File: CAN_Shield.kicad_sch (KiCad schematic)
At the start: 23 parts, among them J1 GPIO, U1 ATECC608A-SSHDA-T, U2 MCP2515T-I/SO, U4 SN65HVD230DR, X1 X322516MLB4SI, j2 DB128V-5.08-5P-GN-S, j3 DB128V-5.08-7P-GN-S, j4 DB128V-5.08-7P-GN-S

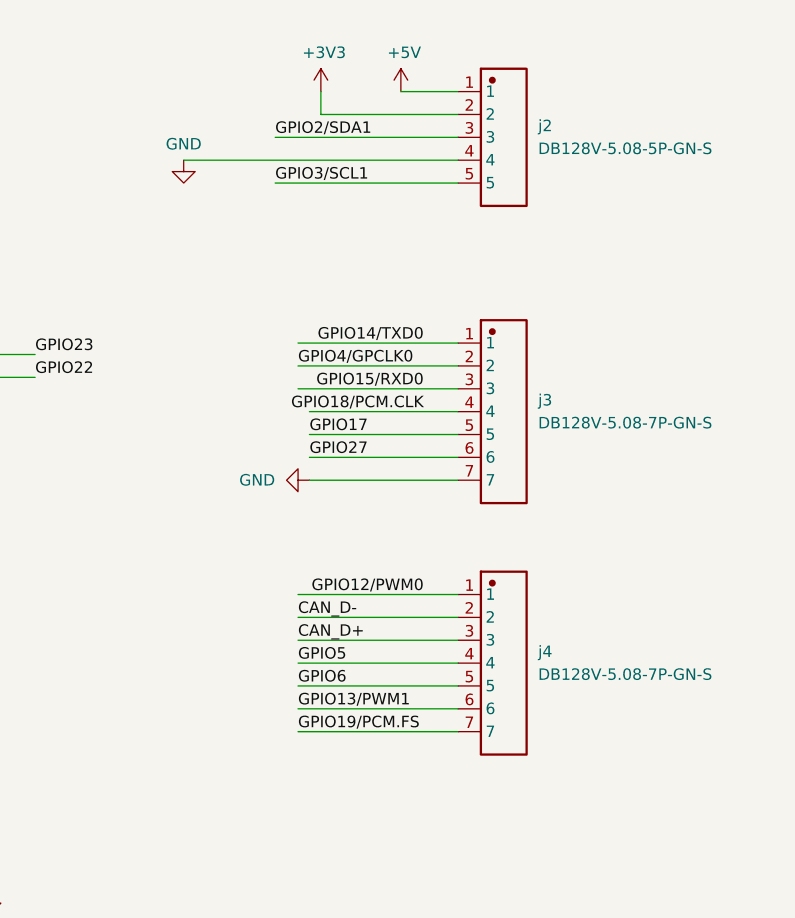
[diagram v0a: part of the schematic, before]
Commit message: Quick fix from EzSeperateI2C
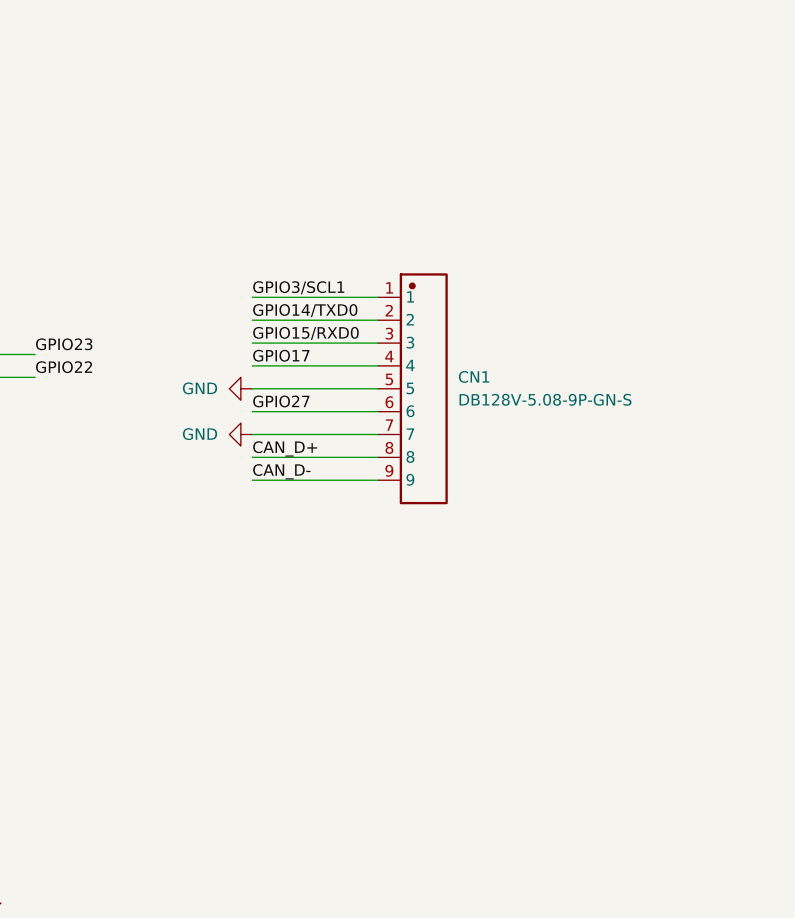
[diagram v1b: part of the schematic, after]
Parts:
- removed j2: DB128V-5.08-5P-GN-S, ImportFP:CONN-TH_5P-P5.08_DIBO_DB128V-5.08-5P-GN-S, symbol ImportSymbol:DB128V-5.08-5P-GN-S
- removed j3, j4: DB128V-5.08-7P-GN-S, ImportFP:CONN-TH_7P-P5.08_DIBO_DB128V-5.08-7P-GN-S, symbol ImportSymbol:DB128V-5.08-7P-GN-S
- added CN1: DB128V-5.08-9P-GN-S, ImportFP:CONN-TH_9P-P5.08_DIBO_DB128V-5.08-9P-GN-S, symbol ImportSymbol:DB128V-5.08-9P-GN-S
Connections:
- net CAN_D+: now also CN1.8
- net CAN_D-: now also CN1.9
- net GND: now also CN1.5, CN1.7
- net GPIO14/TXD0: now also CN1.2
- net GPIO15/RXD0: now also CN1.3
- net GPIO17: now also CN1.4
- net GPIO27: now also CN1.6
- net GPIO3/SCL1: now also CN1.1

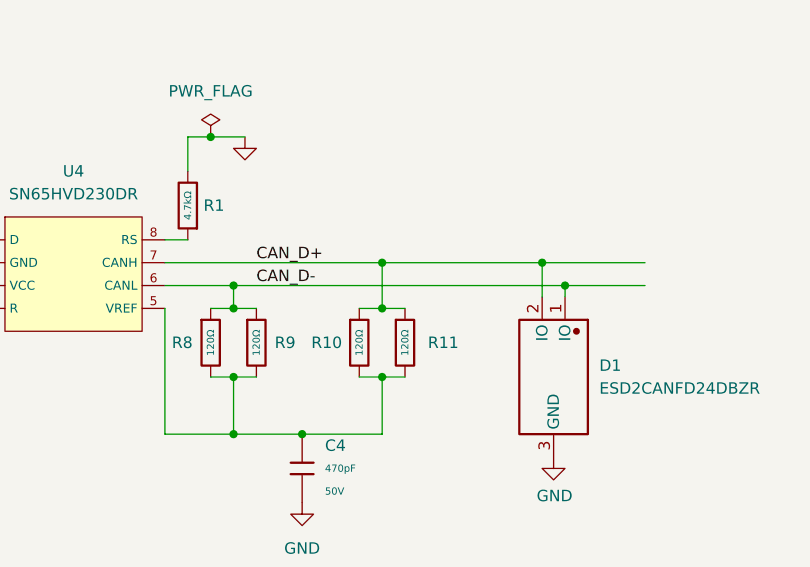
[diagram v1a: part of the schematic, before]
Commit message: Finished DesktopShield layout but still not gen production file
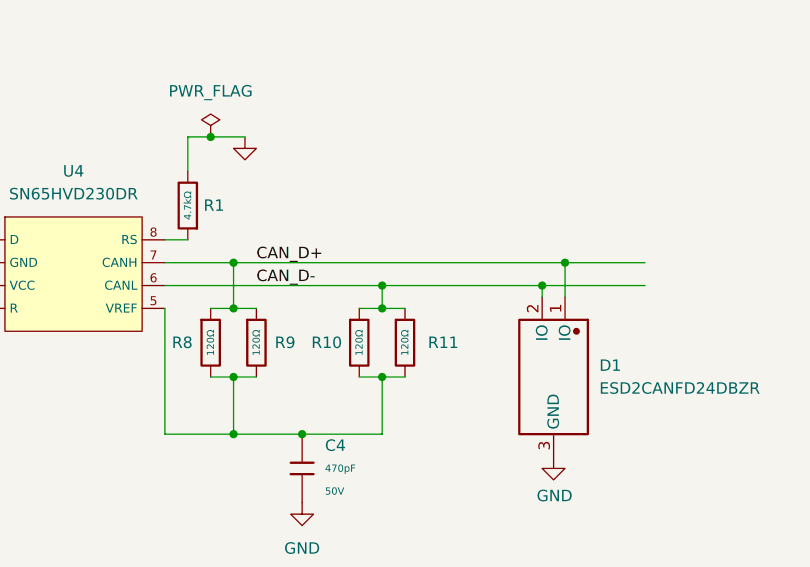
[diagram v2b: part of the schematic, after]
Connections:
- net CAN_D+: now also D1.1 (IO), R8.1, R9.1; no longer D1.2 (IO), R10.1, R11.1
- net CAN_D-: now also D1.2 (IO), R10.1, R11.1; no longer D1.1 (IO), R8.1, R9.1
